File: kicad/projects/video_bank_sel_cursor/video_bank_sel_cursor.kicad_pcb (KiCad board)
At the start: 2 copper layers, 203.2 x 97.8 mm, 41 parts, among them J1 peripheral_addr_bus_connector, J2 peripheral_aux_connector, J3 peripheral_membank_connector, J4 Conn_01x16_Socket, J5 Conn_01x16_Socket, J6 video_aux, J7 Conn_01x16_Socket, J8 Conn_01x06_Socket, U1 74HC245, U10 74HC10, U11 74HC377, U12 74HC377, U14 74HC245, U15 74HC245, U2 74HC245, U3 74HC245, U4 74HC245, U5 74HC245, U6 74HC245, U7 74HC245, U8 74HC245, U9 74HC10

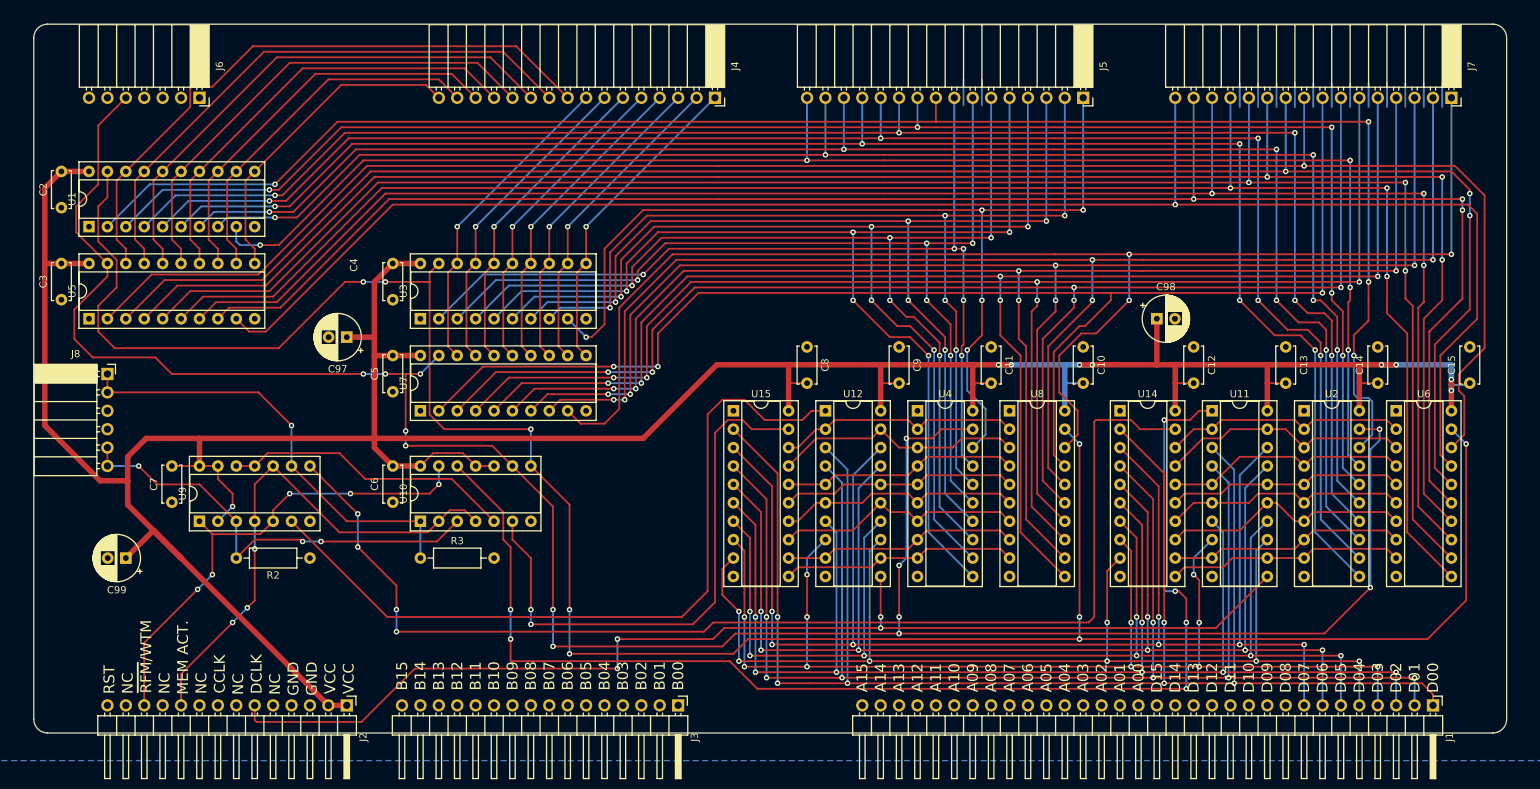
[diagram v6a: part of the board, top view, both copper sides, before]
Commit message: Row and column order made consistent on top connectors. Bank Sel cursor tech checked.
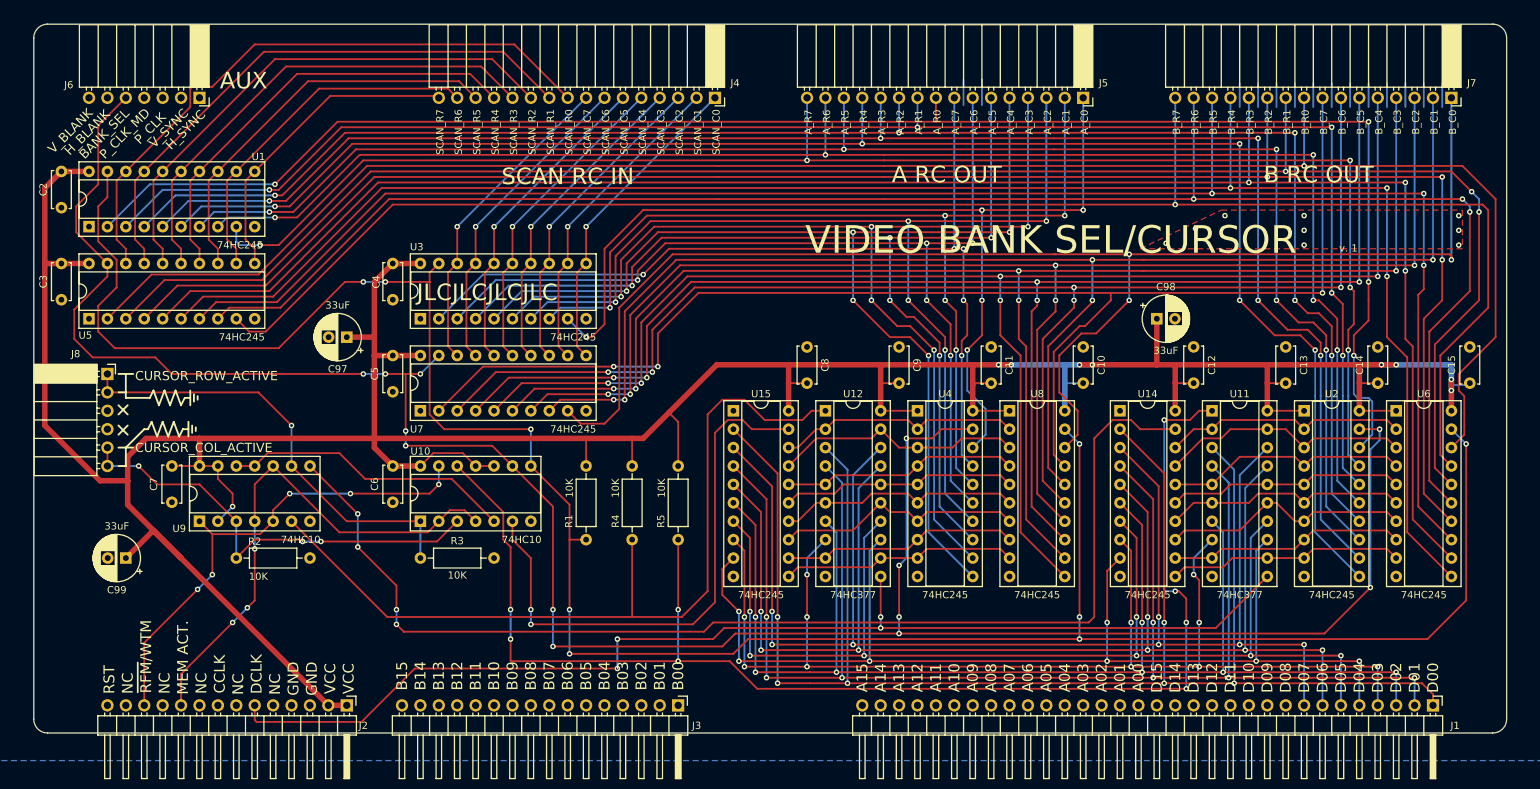
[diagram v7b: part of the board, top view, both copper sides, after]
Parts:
- added R1: 10K, Resistor_THT:R_Axial_DIN0207_L6.3mm_D2.5mm_P10.16mm_Horizontal, F.Cu at (127.0, 121.9)
- added R4: 10K, Resistor_THT:R_Axial_DIN0207_L6.3mm_D2.5mm_P10.16mm_Horizontal, F.Cu at (133.3, 121.9)
- added R5: 10K, Resistor_THT:R_Axial_DIN0207_L6.3mm_D2.5mm_P10.16mm_Horizontal, F.Cu at (139.7, 121.9)
- C97, C98, C99: value C_Polarized -> 33uF
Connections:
- U1 pad 1: unconnected-(U1-DIR-Pad1) -> GND
- U14 pad 1: unconnected-(U14-DIR-Pad1) -> GND
- U15 pad 1: unconnected-(U15-DIR-Pad1) -> GND
- U2 pad 1: unconnected-(U2-DIR-Pad1) -> VCC
- U3 pad 1: unconnected-(U3-DIR-Pad1) -> GND
- U4 pad 1: unconnected-(U4-DIR-Pad1) -> VCC
- U5 pad 1: unconnected-(U5-DIR-Pad1) -> GND
- U6 pad 1: unconnected-(U6-DIR-Pad1) -> VCC
- U7 pad 1: unconnected-(U7-DIR-Pad1) -> GND
- U8 pad 1: unconnected-(U8-DIR-Pad1) -> VCC
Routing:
- net VCC: track 471.2 -> 507.0 mm
- net /~{CURSOR_ROW_WTM}: track 171.3 -> 188.1 mm, vias 6 -> 8
- net /~{CURSOR_COL_WTM}: track 107.5 -> 118.2 mm
- net /OUT_B_ROW_7: track 232.0 -> 234.4 mm
- net /~{BANK_SEL}: track 325.6 -> 327.8 mm
- net /~{CURSOR_ROW_RFM}: track 163.6 -> 161.7 mm
- net /OUT_B_ROW_0: track 247.4 -> 249.2 mm
- net /OUT_B_COL_0: track 196.3 -> 197.6 mm
- net /EXT_ROW_7: track 44.8 -> 43.6 mm
- net /EXT_ROW_6: track 50.5 -> 49.5 mm
- net /OUT_B_ROW_1: track 248.6 -> 249.7 mm
- net /EXT_ROW_5: track 56.3 -> 55.4 mm
- net /OUT_B_ROW_6: track 237.8 -> 238.7 mm
- net /EXT_ROW_4: track 62.0 -> 61.3 mm
- net GND: vias 0 -> 9
- added copper zone on F.Cu, net GND
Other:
- board text added: "A RC OUT"
- board text added: "AUX"
- board text added: "A_C0"
- board text added: "A_C1"
- board text added: "A_C2"
- board text added: "A_C3"
- board text added: "A_C4"
- board text added: "A_C5"
- board text added: "A_C6"
- board text added: "A_C7"
- board text added: "A_R0"
- board text added: "A_R1"
- board text added: "A_R2"
- board text added: "A_R3"
- board text added: "A_R4"
- board text added: "A_R5"
- board text added: "A_R6"
- board text added: "A_R7"
- board text added: "B RC OUT"
- board text added: "BANK_SEL"
- board text added: "B_C0"
- board text added: "B_C1"
- board text added: "B_C2"
- board text added: "B_C3"
- board text added: "B_C4"
- board text added: "B_C5"
- board text added: "B_C6"
- board text added: "B_C7"
- board text added: "B_R0"
- board text added: "B_R1"
- board text added: "B_R2"
- board text added: "B_R3"
- board text added: "B_R4"
- board text added: "B_R5"
- board text added: "B_R6"
- board text added: "B_R7"
- board text added: "CURSOR_COL_ACTIVE"
- board text added: "CURSOR_ROW_ACTIVE"
- board text added: "H_BLANK"
- board text added: "H_SYNC"
- board text added: "JLCJLCJLCJLC"
- board text added: "P_CLK"
- board text added: "P_CLK_MD"
- board text added: "SCAN RC IN"
- board text added: "SCAN_C0"
- board text added: "SCAN_C1"
- board text added: "SCAN_C2"
- board text added: "SCAN_C3"
- board text added: "SCAN_C4"
- board text added: "SCAN_C5"
- board text added: "SCAN_C6"
- board text added: "SCAN_C7"
- board text added: "SCAN_R0"
- board text added: "SCAN_R1"
- board text added: "SCAN_R2"
- board text added: "SCAN_R3"
- board text added: "SCAN_R4"
- board text added: "SCAN_R5"
- board text added: "SCAN_R6"
- board text added: "SCAN_R7"
- board text added: "VIDEO BANK SEL/CURSOR"
- board text added: "V_BLANK"
- board text added: "V_SYNC"
- board text added: "v. 1"

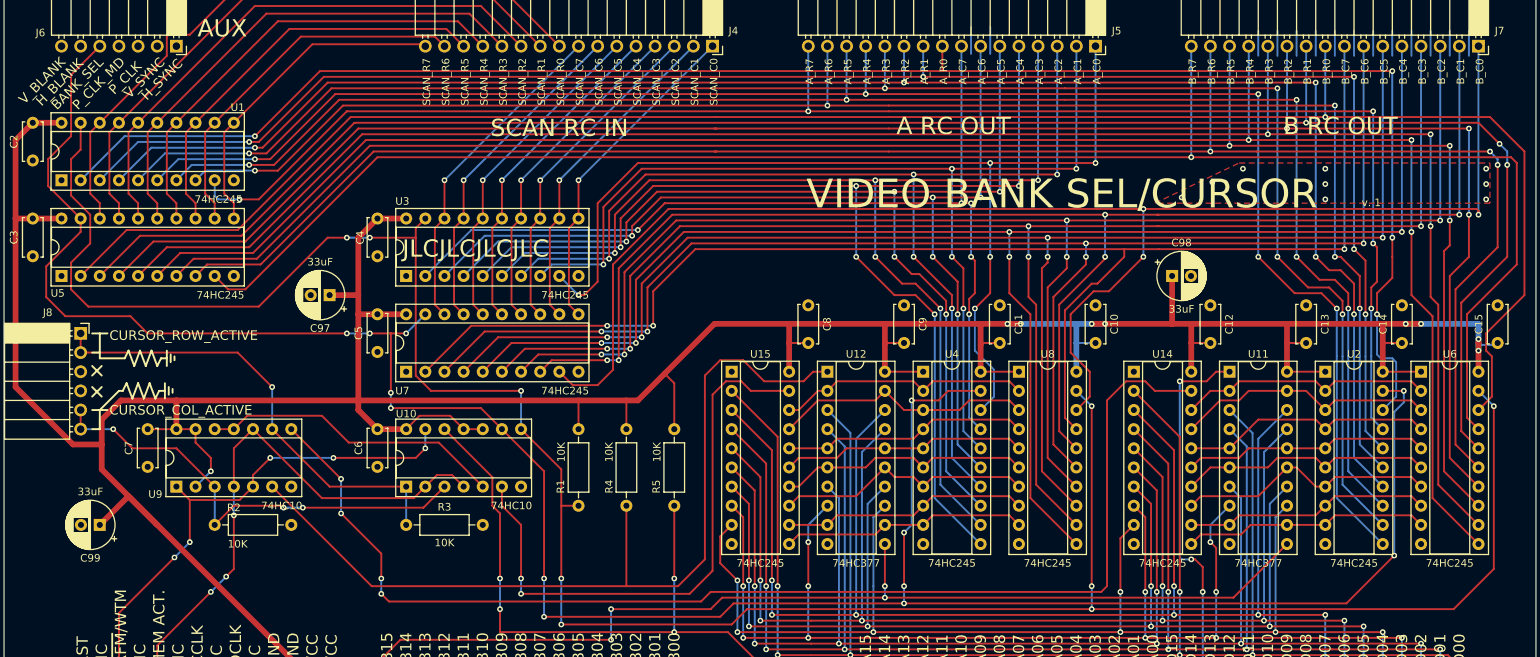
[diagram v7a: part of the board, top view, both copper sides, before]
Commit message: Switched A and B outputs on bank sel. Bit of work on logic and PCB for output. Clarified bank sel 0 and 1 and banks A and B in docs.
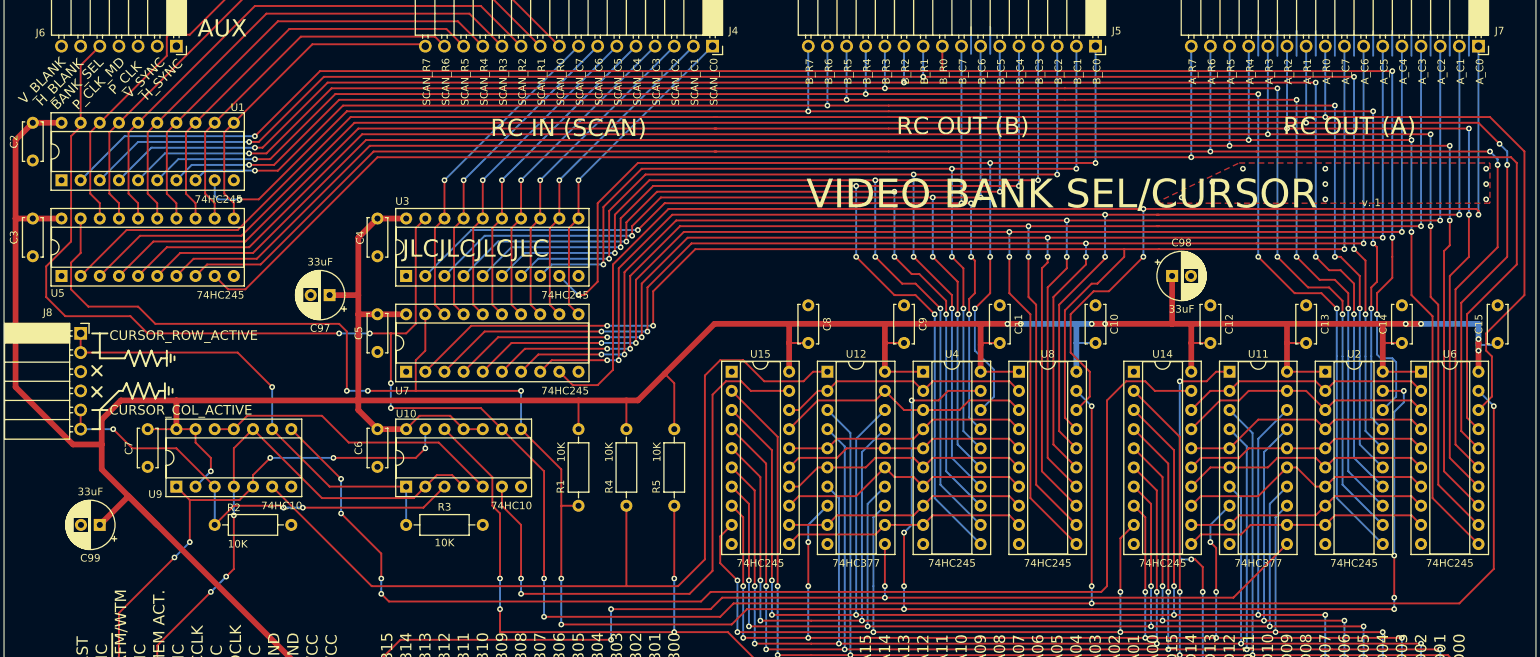
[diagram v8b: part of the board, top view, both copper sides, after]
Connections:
- J5 pad 1: /OUT_A_COL_0 -> /OUT_B_COL_0
- J5 pad 10: /OUT_A_ROW_1 -> /OUT_B_ROW_1
- J5 pad 11: /OUT_A_ROW_2 -> /OUT_B_ROW_2
- J5 pad 12: /OUT_A_ROW_3 -> /OUT_B_ROW_3
- J5 pad 13: /OUT_A_ROW_4 -> /OUT_B_ROW_4
- J5 pad 14: /OUT_A_ROW_5 -> /OUT_B_ROW_5
- J5 pad 15: /OUT_A_ROW_6 -> /OUT_B_ROW_6
- J5 pad 16: /OUT_A_ROW_7 -> /OUT_B_ROW_7
- J5 pad 2: /OUT_A_COL_1 -> /OUT_B_COL_1
- J5 pad 3: /OUT_A_COL_2 -> /OUT_B_COL_2
- J5 pad 4: /OUT_A_COL_3 -> /OUT_B_COL_3
- J5 pad 5: /OUT_A_COL_4 -> /OUT_B_COL_4
- J5 pad 6: /OUT_A_COL_5 -> /OUT_B_COL_5
- J5 pad 7: /OUT_A_COL_6 -> /OUT_B_COL_6
- J5 pad 8: /OUT_A_COL_7 -> /OUT_B_COL_7
- J5 pad 9: /OUT_A_ROW_0 -> /OUT_B_ROW_0
- J7 pad 1: /OUT_B_COL_0 -> /OUT_A_COL_0
- J7 pad 10: /OUT_B_ROW_1 -> /OUT_A_ROW_1
- J7 pad 11: /OUT_B_ROW_2 -> /OUT_A_ROW_2
- J7 pad 12: /OUT_B_ROW_3 -> /OUT_A_ROW_3
- J7 pad 13: /OUT_B_ROW_4 -> /OUT_A_ROW_4
- J7 pad 14: /OUT_B_ROW_5 -> /OUT_A_ROW_5
- J7 pad 15: /OUT_B_ROW_6 -> /OUT_A_ROW_6
- J7 pad 16: /OUT_B_ROW_7 -> /OUT_A_ROW_7
- J7 pad 2: /OUT_B_COL_1 -> /OUT_A_COL_1
- J7 pad 3: /OUT_B_COL_2 -> /OUT_A_COL_2
- J7 pad 4: /OUT_B_COL_3 -> /OUT_A_COL_3
- J7 pad 5: /OUT_B_COL_4 -> /OUT_A_COL_4
- J7 pad 6: /OUT_B_COL_5 -> /OUT_A_COL_5
- J7 pad 7: /OUT_B_COL_6 -> /OUT_A_COL_6
- J7 pad 8: /OUT_B_COL_7 -> /OUT_A_COL_7
- J7 pad 9: /OUT_B_ROW_0 -> /OUT_A_ROW_0
- U1 pad 19: /~{BANK_SEL} -> /BANK_SEL
- U1 pad 2: /OUT_A_ROW_0 -> /OUT_B_ROW_0
- U1 pad 3: /OUT_A_ROW_1 -> /OUT_B_ROW_1
- U1 pad 4: /OUT_A_ROW_2 -> /OUT_B_ROW_2
- U1 pad 5: /OUT_A_ROW_3 -> /OUT_B_ROW_3
- U1 pad 6: /OUT_A_ROW_4 -> /OUT_B_ROW_4
- U1 pad 7: /OUT_A_ROW_5 -> /OUT_B_ROW_5
- U1 pad 8: /OUT_A_ROW_6 -> /OUT_B_ROW_6
- U1 pad 9: /OUT_A_ROW_7 -> /OUT_B_ROW_7
- U2 pad 11: /OUT_A_ROW_4 -> /OUT_B_ROW_4
- U2 pad 12: /OUT_A_ROW_3 -> /OUT_B_ROW_3
- U2 pad 13: /OUT_A_ROW_5 -> /OUT_B_ROW_5
- U2 pad 14: /OUT_A_ROW_2 -> /OUT_B_ROW_2
- U2 pad 15: /OUT_A_ROW_6 -> /OUT_B_ROW_6
- U2 pad 16: /OUT_A_ROW_1 -> /OUT_B_ROW_1
- U2 pad 17: /OUT_A_ROW_7 -> /OUT_B_ROW_7
- U2 pad 18: /OUT_A_ROW_0 -> /OUT_B_ROW_0
- U2 pad 19: /BANK_SEL -> /~{BANK_SEL}
- U3 pad 19: /~{BANK_SEL} -> /BANK_SEL
- U3 pad 2: /OUT_A_COL_7 -> /OUT_B_COL_7
- U3 pad 3: /OUT_A_COL_6 -> /OUT_B_COL_6
- U3 pad 4: /OUT_A_COL_5 -> /OUT_B_COL_5
- U3 pad 5: /OUT_A_COL_4 -> /OUT_B_COL_4
- U3 pad 6: /OUT_A_COL_3 -> /OUT_B_COL_3
- U3 pad 7: /OUT_A_COL_2 -> /OUT_B_COL_2
- U3 pad 8: /OUT_A_COL_1 -> /OUT_B_COL_1
- U3 pad 9: /OUT_A_COL_0 -> /OUT_B_COL_0
- U4 pad 11: /OUT_A_COL_4 -> /OUT_B_COL_4
- U4 pad 12: /OUT_A_COL_3 -> /OUT_B_COL_3
- U4 pad 13: /OUT_A_COL_5 -> /OUT_B_COL_5
- U4 pad 14: /OUT_A_COL_2 -> /OUT_B_COL_2
- U4 pad 15: /OUT_A_COL_6 -> /OUT_B_COL_6
- U4 pad 16: /OUT_A_COL_1 -> /OUT_B_COL_1
- U4 pad 17: /OUT_A_COL_7 -> /OUT_B_COL_7
- U4 pad 18: /OUT_A_COL_0 -> /OUT_B_COL_0
- U4 pad 19: /BANK_SEL -> /~{BANK_SEL}
- U5 pad 19: /BANK_SEL -> /~{BANK_SEL}
- U5 pad 2: /OUT_B_ROW_0 -> /OUT_A_ROW_0
- U5 pad 3: /OUT_B_ROW_1 -> /OUT_A_ROW_1
- U5 pad 4: /OUT_B_ROW_2 -> /OUT_A_ROW_2
- U5 pad 5: /OUT_B_ROW_3 -> /OUT_A_ROW_3
- U5 pad 6: /OUT_B_ROW_4 -> /OUT_A_ROW_4
- U5 pad 7: /OUT_B_ROW_5 -> /OUT_A_ROW_5
- U5 pad 8: /OUT_B_ROW_6 -> /OUT_A_ROW_6
- U5 pad 9: /OUT_B_ROW_7 -> /OUT_A_ROW_7
- U6 pad 11: /OUT_B_ROW_4 -> /OUT_A_ROW_4
- U6 pad 12: /OUT_B_ROW_3 -> /OUT_A_ROW_3
- U6 pad 13: /OUT_B_ROW_5 -> /OUT_A_ROW_5
- U6 pad 14: /OUT_B_ROW_2 -> /OUT_A_ROW_2
- U6 pad 15: /OUT_B_ROW_6 -> /OUT_A_ROW_6
- U6 pad 16: /OUT_B_ROW_1 -> /OUT_A_ROW_1
- U6 pad 17: /OUT_B_ROW_7 -> /OUT_A_ROW_7
- U6 pad 18: /OUT_B_ROW_0 -> /OUT_A_ROW_0
- U6 pad 19: /~{BANK_SEL} -> /BANK_SEL
- U7 pad 19: /BANK_SEL -> /~{BANK_SEL}
- U7 pad 2: /OUT_B_COL_7 -> /OUT_A_COL_7
- U7 pad 3: /OUT_B_COL_6 -> /OUT_A_COL_6
- U7 pad 4: /OUT_B_COL_5 -> /OUT_A_COL_5
- U7 pad 5: /OUT_B_COL_4 -> /OUT_A_COL_4
- U7 pad 6: /OUT_B_COL_3 -> /OUT_A_COL_3
- U7 pad 7: /OUT_B_COL_2 -> /OUT_A_COL_2
- U7 pad 8: /OUT_B_COL_1 -> /OUT_A_COL_1
- U7 pad 9: /OUT_B_COL_0 -> /OUT_A_COL_0
- U8 pad 11: /OUT_B_COL_4 -> /OUT_A_COL_4
- U8 pad 12: /OUT_B_COL_3 -> /OUT_A_COL_3
- U8 pad 13: /OUT_B_COL_5 -> /OUT_A_COL_5
- U8 pad 14: /OUT_B_COL_2 -> /OUT_A_COL_2
- U8 pad 15: /OUT_B_COL_6 -> /OUT_A_COL_6
- U8 pad 16: /OUT_B_COL_1 -> /OUT_A_COL_1
- U8 pad 17: /OUT_B_COL_7 -> /OUT_A_COL_7
- U8 pad 18: /OUT_B_COL_0 -> /OUT_A_COL_0
- U8 pad 19: /~{BANK_SEL} -> /BANK_SEL
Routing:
- net /OUT_B_COL_0: track 197.6 -> 136.4 mm, vias 3 -> 5
- net /OUT_A_COL_0: track 136.4 -> 197.6 mm, vias 5 -> 3
- net /OUT_B_COL_1: track 194.8 -> 136.4 mm
- net /OUT_A_COL_1: track 136.4 -> 194.8 mm
- net /OUT_B_COL_7: track 186.5 -> 128.3 mm, vias 3 -> 5
- net /OUT_A_COL_7: track 128.3 -> 186.5 mm, vias 5 -> 3
- net /OUT_B_COL_6: track 191.3 -> 134.7 mm
- net /OUT_A_COL_6: track 134.7 -> 191.3 mm
- net /OUT_B_COL_2: track 197.7 -> 142.5 mm
- net /OUT_A_COL_2: track 142.5 -> 197.7 mm
- net /OUT_B_COL_5: track 196.6 -> 143.5 mm
- net /OUT_A_COL_5: track 143.5 -> 196.6 mm
- net /OUT_B_COL_3: track 202.0 -> 149.7 mm
- net /OUT_A_COL_3: track 149.7 -> 202.0 mm
- net /OUT_B_COL_4: track 204.2 -> 152.8 mm
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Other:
- board text added: "RC IN (SCAN)"
- board text added: "RC OUT (A)"
- board text added: "RC OUT (B)"
- board text removed: "A RC OUT"
- board text removed: "B RC OUT"
- board text removed: "SCAN RC IN"
